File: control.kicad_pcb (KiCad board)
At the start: 2 copper layers, 182 parts, among them J1 Wurth_THR_Terminal_M4, J10 TE_Faston_20-16AWG_Straight_T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, J11 TE_Faston_20-16AWG_Straight_T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, J12 TE_Faston_20-16AWG_Straight_T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, J13 TE_Faston_20-16AWG_Straight_T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, J14 TE_Faston_20-16AWG_Straight_T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, J15 TE_Faston_20-16AWG_Straight_T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, J16 TE_Faston_20-16AWG_Straight_T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, J17 TE_Faston_20-16AWG_Straight_T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, J18 TE_Faston_20-16AWG_Straight_T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, J19 TE_Faston_20-16AWG_Straight_T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, J2 Wurth_THR_Terminal_M4, J20 TE_Faston_20-16AWG_Straight_T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, J21 TE_Faston_20-16AWG_Straight_T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, J22 TE_Faston_20-16AWG_Straight_T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, J23 TE_Faston_20-16AWG_Straight_T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, J24 TE_Faston_20-16AWG_Straight_T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, J25 TE_Faston_20-16AWG_Straight_T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, J26 TE_Faston_20-16AWG_Straight_T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, J27 TE_Faston_20-16AWG_Straight_T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, J28 TE_Faston_20-16AWG_Straight_T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, J29 TE_Faston_20-16AWG_Straight_T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, J3 Wurth_THR_Terminal_M4, J30 TE_Faston_20-16AWG_Straight_T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, J31 TE_Faston_20-16AWG_Straight_T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, J32 TE_Faston_20-16AWG_Straight_T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, J33 Conn_ARM_JTAG_SWD_10, J34 TE_Faston_20-16AWG_Straight_T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, J35 TE_Faston_20-16AWG_Straight_T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, J36 TE_Faston_20-16AWG_Straight_T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, J37 TE_Faston_20-16AWG_Straight_T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, J38 TE_Faston_20-16AWG_Straight_T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, J39 TE_Faston_20-16AWG_Straight_T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, J4 Conn_01x03, J40 TE_Faston_20-16AWG_Straight_T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, J41 TE_Faston_20-16AWG_Straight_T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, J42 TE_Faston_20-16AWG_Straight_T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, J43 TE_Faston_20-16AWG_Straight_T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, J5 Conn_02x20_Odd_Even, J6 TE_Faston_20-16AWG_Straight_T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, J7 TE_Faston_20-16AWG_Straight_T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, J8 TE_Faston_20-16AWG_Straight_T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, J9 TE_Faston_20-16AWG_Straight_T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, Q1 ZXTN08400BFFCT, SW1 SW_Push, U1 TPS7B8733, U10 VND5160J, U11 VND5160J, U12 TCMT4600, U13 TCMT4600, U14 ATSAMD21J18A-A, U15 TCMT4600, U16 VND5160J, U17 VND5160J, U18 VND5160J, U2 MAX33071, U3 TCMT4600, U4 VND5160J, U5 VND5160J, U6 VND5160J, U7 VND5160J, U8 VND5160J, U9 VND5160J, Y1 Crystal

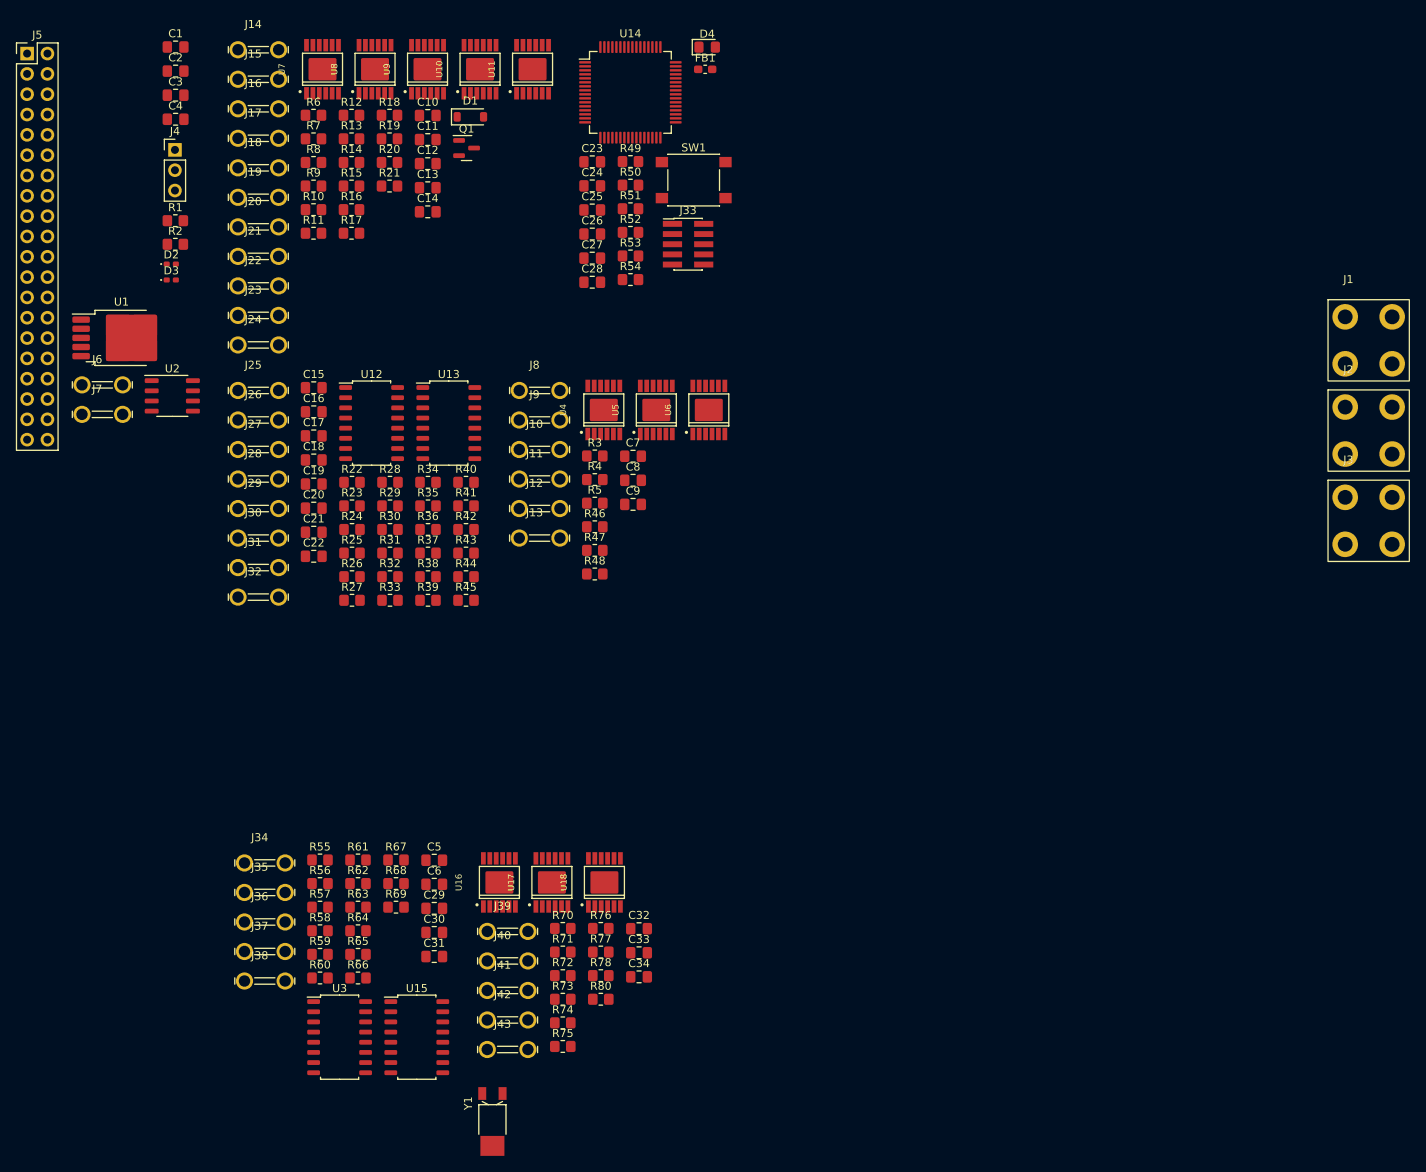
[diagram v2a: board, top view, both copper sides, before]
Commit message: connect signals to connectors, start layout
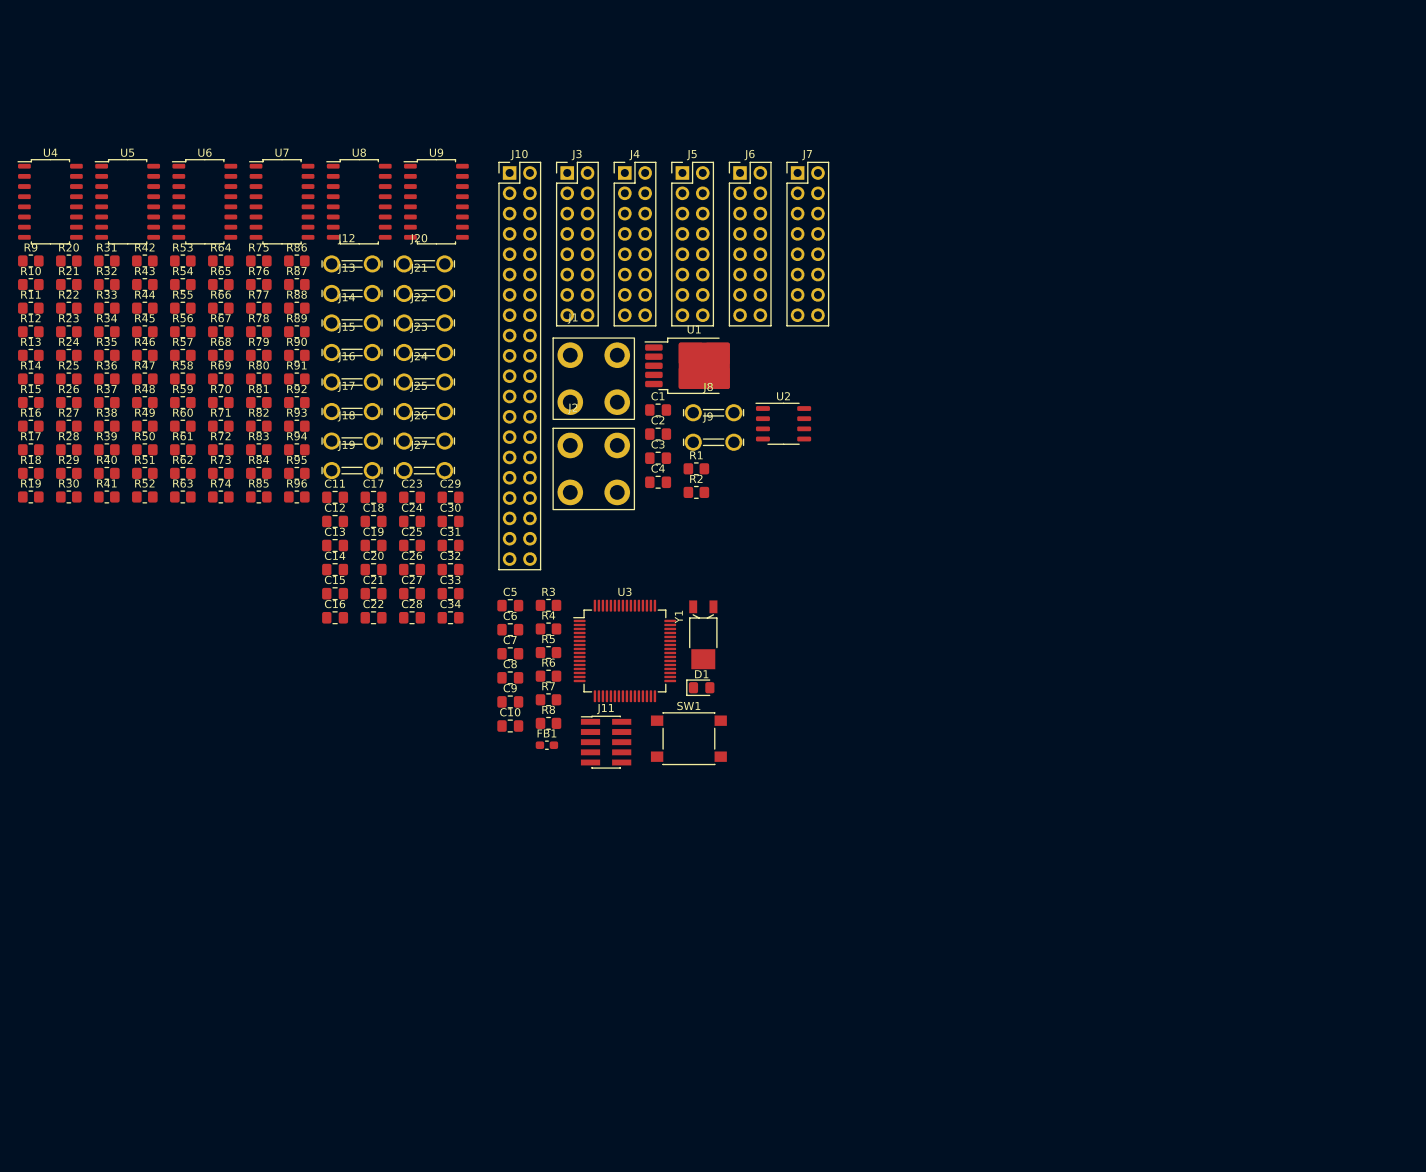
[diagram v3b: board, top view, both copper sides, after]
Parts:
- removed D2, D3: D15V0HA1U2LP-7B, Diode_SMD:D_0402_1005Metric_Pad0.77x0.64mm_HandSolder
- removed D4: LED, LED_SMD:LED_0805_2012Metric_Pad1.15x1.40mm_HandSolder
- removed J28, J29, J30, J31, J32, J34, J35, J36, J37, J38, J39, J40, J41, J42, J43: TE_Faston_20-16AWG_Straight_Tab, Toadly:TE_Faston_20-16AWG_Straight_Tab
- removed J33: Conn_ARM_JTAG_SWD_10, Connector_PinHeader_1.27mm:PinHeader_2x05_P1.27mm_Vertical_SMD
- removed Q1: ZXTN08400BFFCT, Package_TO_SOT_SMD:SOT-23
- removed U10, U11, U16, U17, U18: VND5160J, Toadly:POWERSSO-12
- removed U12, U13, U15: TCMT4600, Package_SO:SOP-16_4.55x10.3mm_P1.27mm
- removed U14: ATSAMD21J18A-A, Package_QFP:TQFP-64_10x10mm_P0.5mm
- added R79: DNP, Resistor_SMD:R_0805_2012Metric_Pad1.20x1.40mm_HandSolder, F.Cu at (-81.4, 43.0)
- added R81: DNP, Resistor_SMD:R_0805_2012Metric_Pad1.20x1.40mm_HandSolder, F.Cu at (-81.4, 48.9)
- added R82: 3.3k, Resistor_SMD:R_0805_2012Metric_Pad1.20x1.40mm_HandSolder, F.Cu at (-81.4, 51.8)
- added R83: 3.3k, Resistor_SMD:R_0805_2012Metric_Pad1.20x1.40mm_HandSolder, F.Cu at (-81.4, 54.8)
- added R84: 3.3k, Resistor_SMD:R_0805_2012Metric_Pad1.20x1.40mm_HandSolder, F.Cu at (-81.4, 57.7)
- added R85: DNP, Resistor_SMD:R_0805_2012Metric_Pad1.20x1.40mm_HandSolder, F.Cu at (-81.4, 60.7)
- added R86: 1.1k, Resistor_SMD:R_0805_2012Metric_Pad1.20x1.40mm_HandSolder, F.Cu at (-76.6, 31.2)
- added R87: DNP, Resistor_SMD:R_0805_2012Metric_Pad1.20x1.40mm_HandSolder, F.Cu at (-76.6, 34.1)
- added R88: 1.1k, Resistor_SMD:R_0805_2012Metric_Pad1.20x1.40mm_HandSolder, F.Cu at (-76.6, 37.1)
- added R89: DNP, Resistor_SMD:R_0805_2012Metric_Pad1.20x1.40mm_HandSolder, F.Cu at (-76.6, 40.0)
- added R90: 1.1k, Resistor_SMD:R_0805_2012Metric_Pad1.20x1.40mm_HandSolder, F.Cu at (-76.6, 43.0)
- added R91: DNP, Resistor_SMD:R_0805_2012Metric_Pad1.20x1.40mm_HandSolder, F.Cu at (-76.6, 45.9)
- added R92: 1.1k, Resistor_SMD:R_0805_2012Metric_Pad1.20x1.40mm_HandSolder, F.Cu at (-76.6, 48.9)
- added R93: DNP, Resistor_SMD:R_0805_2012Metric_Pad1.20x1.40mm_HandSolder, F.Cu at (-76.6, 51.8)
- added R94: 1.1k, Resistor_SMD:R_0805_2012Metric_Pad1.20x1.40mm_HandSolder, F.Cu at (-76.6, 54.8)
- added R95: DNP, Resistor_SMD:R_0805_2012Metric_Pad1.20x1.40mm_HandSolder, F.Cu at (-76.6, 57.7)
- added R96: 1.1k, Resistor_SMD:R_0805_2012Metric_Pad1.20x1.40mm_HandSolder, F.Cu at (-76.6, 60.7)
- C10: value DNP -> 10uF/16V
- C11, C12, C13, C14, C32, C33, C34: value DNP -> 1uF
- C23, C24, C28: value 0.1uF -> 1uF
- C25, C26: value 6.8pF -> 1uF
- C27: value 10uF/16V -> 1uF
- C5, C6: value 1uF -> 6.8pF
- C7, C8, C9: value DNP -> 0.1uF
- D1: value 1N4148W -> LED; footprint Diode_SMD:D_SOD-123 -> LED_SMD:LED_0805_2012Metric_Pad1.15x1.40mm_HandSolder
- J10: value TE_Faston_20-16AWG_Straight_Tab -> Conn_02x20_Odd_Even; footprint Toadly:TE_Faston_20-16AWG_Straight_Tab -> Connector_PinHeader_2.54mm:PinHeader_2x20_P2.54mm_Vertical
- J11: value TE_Faston_20-16AWG_Straight_Tab -> Conn_ARM_JTAG_SWD_10; footprint Toadly:TE_Faston_20-16AWG_Straight_Tab -> Connector_PinHeader_1.27mm:PinHeader_2x05_P1.27mm_Vertical_SMD
- J3: value Wurth_THR_Terminal_M4 -> Conn_02x08_Odd_Even; footprint Toadly:Wurth_THR_Terminal_M4 -> Connector_PinHeader_2.54mm:PinHeader_2x08_P2.54mm_Vertical
- J4: value Conn_01x03 -> Conn_02x08_Odd_Even; footprint Connector_PinHeader_2.54mm:PinHeader_1x03_P2.54mm_Vertical -> Connector_PinHeader_2.54mm:PinHeader_2x08_P2.54mm_Vertical
- J5: value Conn_02x20_Odd_Even -> Conn_02x08_Odd_Even; footprint Connector_PinHeader_2.54mm:PinHeader_2x20_P2.54mm_Vertical -> Connector_PinHeader_2.54mm:PinHeader_2x08_P2.54mm_Vertical
- J6, J7: value TE_Faston_20-16AWG_Straight_Tab -> Conn_02x08_Odd_Even; footprint Toadly:TE_Faston_20-16AWG_Straight_Tab -> Connector_PinHeader_2.54mm:PinHeader_2x08_P2.54mm_Vertical
- R1: value 120 -> 10K
- R10, R11, R12, R15, R16, R75, R77, R78, R9: value 10k -> 3.3k
- R13, R14, R17, R19, R21, R47, R5, R71, R73, R74, R76, R80: value 10k -> DNP
- R18, R20, R46, R48, R70, R72: value 10k -> 1.1k
- R2: value 10K -> 120
- R22, R24: value 3.3k -> 1.1k
- R23, R25, R34, R37, R67: value 3.3k -> DNP
- R26, R28, R38, R40, R42, R44, R68: value DNP -> 1.1k
- R27, R33, R39, R41, R43, R45, R69: value 1.1k -> DNP
- R29, R31, R60: value 1.1k -> 3.3k
- R3: value 10k -> 100K
- R30, R32, R59: value DNP -> 3.3k
- R4, R7: value 10k -> 39
- R49, R54: value 39 -> DNP
- R50: value 0 -> DNP
- R52: value 91 -> DNP
- R53: value 100K -> DNP
- R6: value 10k -> 0
- R8: value 10k -> 91
- U3: value TCMT4600 -> ATSAMD21J18A-A; footprint Package_SO:SOP-16_4.55x10.3mm_P1.27mm -> Package_QFP:TQFP-64_10x10mm_P0.5mm
- U4, U5, U6, U7, U8, U9: value VND5160J -> TCMT4600; footprint Toadly:POWERSSO-12 -> Package_SO:SOP-16_4.55x10.3mm_P1.27mm
- moved J3 109.2 mm to (-42.8, 20.2)
- moved R75 105.3 mm to (-81.4, 31.2)
- moved J1 97.0 mm to (-39.5, 45.9)
- moved J2 97.0 mm to (-39.5, 57.2)
- moved J7 92.0 mm to (-14.0, 20.2)
- moved R76 91.1 mm to (-81.4, 34.1)
- moved R77 91.1 mm to (-81.4, 37.1)
- moved R78 91.1 mm to (-81.4, 40.0)
- moved R80 88.5 mm to (-81.4, 45.9)
- moved FB1 86.8 mm to (-45.4, 91.7)
- moved R64 85.5 mm to (-86.1, 31.2)
- moved R65 85.5 mm to (-86.1, 34.1)
- moved R66 85.5 mm to (-86.1, 37.1)
- moved J6 84.0 mm to (-21.2, 20.2)
- moved J5 83.3 mm to (-28.4, 20.2)
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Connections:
- C10 pad 1: +12C -> GNDREF
- C10 pad 2: GNDREF -> Net-(U3-VDDANA)
- C11 pad 1: +12C -> STOP_LIGHT_SENSE
- C12 pad 1: +12C -> PARK_BRAKE_SENSE
- C13 pad 1: +12C -> MARKER_LIGHT_SENSE
- C14 pad 1: +12C -> REVERSE_LIGHT_SENSE
- C15 pad 1: /Signals/STOP_LIGHT_SENSE -> CAB_2_SENSE
- C16 pad 1: /Signals/PARK_BRAKE_SENSE -> CAB_1_SENSE
- C17 pad 1: /Signals/MARKER_LIGHT_SENSE -> HORN_SENSE
- C18 pad 1: /Signals/REVERSE_LIGHT_SENSE -> AUX_1_SENSE
- C19 pad 1: /Signals/REAR_DOOR_SENSE -> AUX_2_SENSE
- C20 pad 1: /Signals/SIDE_DOOR_SENSE -> BATT_SW_SENSE
- C21 pad 1: /Signals/HORN_SENSE -> CAB_4_SENSE
- C22 pad 1: /Signals/BATT_SW_SENSE -> CAB_3_SENSE
- C23 pad 1: +3.3V -> CAB_6_SENSE
- C24 pad 1: Net-(U14-VDDCORE) -> CAB_5_SENSE
- C25 pad 1: GNDREF -> REAR_DOOR_SENSE
- C25 pad 2: Net-(U14-PA00) -> GNDREF
- C26 pad 1: GNDREF -> COMP_5_SENSE
- C26 pad 2: Net-(U14-PA01) -> GNDREF
- C27 pad 1: GNDREF -> COMP_1_SENSE
- C27 pad 2: Net-(U14-VDDANA) -> GNDREF
- C28 pad 1: GNDREF -> COMP_2_SENSE
- C28 pad 2: Net-(U14-VDDANA) -> GNDREF
- C29 pad 1: /Signals/COMP_2_SENSE -> CAB_8_SENSE
- C30 pad 1: /Signals/COMP_3_SENSE -> CAB_7_SENSE
- C31 pad 1: /Signals/COMP_5_SENSE -> AUX_3_SENSE
- C32 pad 1: +12V -> SIDE_DOOR_SENSE
- C33 pad 1: +12V -> COMP_4_SENSE
- C34 pad 1: +12V -> COMP_3_SENSE
- C5 pad 1: /Signals/COMP_4_SENSE -> GNDREF
- C5 pad 2: GNDREF -> Net-(U3-PA01)
- C6 pad 1: /Signals/COMP_1_SENSE -> GNDREF
- C6 pad 2: GNDREF -> Net-(U3-PA00)
- C7 pad 1: +12V -> Net-(U3-VDDCORE)
- C8 pad 1: +12V -> +3.3V
- C9 pad 1: +12V -> GNDREF
- C9 pad 2: GNDREF -> Net-(U3-VDDANA)
- D1 pad 1: +12C -> Net-(D1-K)
- FB1 pad 1: Net-(U14-VDDANA) -> Net-(U3-VDDANA)
- J10 pad 1: Net-(J10-P1-Pad1) -> +12V
- J10 pad 2: Net-(J10-P1-Pad1) -> +12V
- J11 pad 1: Net-(J11-P1-Pad1) -> Net-(J11-VTref)
- J11 pad 2: Net-(J11-P1-Pad1) -> /MCU/SWDIO
- J2 pad 1: +12C -> GNDREF
- J20 pad 1: Net-(D1-A) -> Net-(J20-P1-Pad1)
- J20 pad 2: Net-(D1-A) -> Net-(J20-P1-Pad1)
- J3 pad 1: GNDREF -> unconnected-(J3-Pin_1-Pad1)
- J4 pad 1: /HORN_SENSE -> unconnected-(J4-Pin_1-Pad1)
- J4 pad 2: /Truck Drivers/HORN_EN -> unconnected-(J4-Pin_2-Pad2)
- J4 pad 3: /HORN_CTL -> unconnected-(J4-Pin_3-Pad3)
- J5 pad 1: +12V -> unconnected-(J5-Pin_1-Pad1)
- J5 pad 10: /RS485_B -> COMP_3_LGT_EN
- J5 pad 12: unconnected-(J5-Pin_12-Pad12) -> COMP_4_LGT_EN
- J5 pad 14: unconnected-(J5-Pin_14-Pad14) -> COMP_5_LGT_EN
- J5 pad 2: +12V -> unconnected-(J5-Pin_2-Pad2)
- J5 pad 3: +12V -> unconnected-(J5-Pin_3-Pad3)
- J5 pad 4: +12V -> unconnected-(J5-Pin_4-Pad4)
- J5 pad 5: GNDREF -> unconnected-(J5-Pin_5-Pad5)
- J5 pad 6: GNDREF -> COMP_1_LGT_EN
- J5 pad 7: GNDREF -> unconnected-(J5-Pin_7-Pad7)
- J5 pad 8: GNDREF -> COMP_2_LGT_EN
- J5 pad 9: /RS485_A -> unconnected-(J5-Pin_9-Pad9)
- J6 pad 1: /RS485_A -> unconnected-(J6-Pin_1-Pad1)
- J6 pad 2: /RS485_A -> unconnected-(J6-Pin_2-Pad2)
- J7 pad 1: /RS485_B -> unconnected-(J7-Pin_1-Pad1)
- J7 pad 2: /RS485_B -> unconnected-(J7-Pin_2-Pad2)
- J8 pad 1: Net-(J8-P1-Pad1) -> /RS485_A
- J8 pad 2: Net-(J8-P1-Pad1) -> /RS485_A
- J9 pad 1: Net-(J9-P1-Pad1) -> /RS485_B
- J9 pad 2: Net-(J9-P1-Pad1) -> /RS485_B
- R1 pad 1: /RS485_A -> RS485_DATA_ENABLE
- R1 pad 2: /RS485_B -> GNDREF
- R10 pad 1: GNDREF -> Net-(J13-P1-Pad1)
- R10 pad 2: /Truck Drivers/INTERSECT_P_EN -> Net-(R10-Pad2)
- R11 pad 1: /Truck Drivers/FOG_EN -> Net-(J14-P1-Pad1)
- R11 pad 2: Net-(U8B-EN) -> Net-(R11-Pad2)
- R12 pad 1: /Truck Drivers/CHIME_EN -> Net-(J15-P1-Pad1)
- R12 pad 2: Net-(U7B-EN) -> Net-(R12-Pad2)
- R13 pad 1: /Truck Drivers/BACKUP_EN -> Net-(R13-Pad1)
- R13 pad 2: Net-(U7C-EN) -> CAB_SIGNAL_2
- R14 pad 1: /Truck Drivers/INTERSECT_D_EN -> Net-(R14-Pad1)
- R14 pad 2: Net-(U9B-EN) -> CAB_SIGNAL_1
- R15 pad 1: /Truck Drivers/INTERSECT_P_EN -> Net-(R13-Pad1)
- R15 pad 2: Net-(U9C-EN) -> +12V
- R16 pad 1: /Truck Drivers/HORN_EN -> Net-(R14-Pad1)
- R16 pad 2: Net-(Q1-B) -> +12V
- R17 pad 1: GNDREF -> STOP_LIGHT_SENSE
- R17 pad 2: /Truck Drivers/MARKER_EN -> +3.3V
- R18 pad 2: /Truck Drivers/HEADLIGHT_EN -> STOP_LIGHT_SENSE
- R19 pad 1: Net-(Q1-B) -> PARK_BRAKE_SENSE
- R19 pad 2: GNDREF -> +3.3V
- R2 pad 1: /MCU/RS485_DATA_ENABLE -> /RS485_A
- R2 pad 2: GNDREF -> /RS485_B
- R20 pad 1: /Truck Drivers/MARKER_EN -> GNDREF
- R20 pad 2: Net-(U10B-EN) -> PARK_BRAKE_SENSE
- R21 pad 1: /Truck Drivers/HEADLIGHT_EN -> MARKER_LIGHT_SENSE
- R21 pad 2: Net-(U11B-EN) -> +3.3V
- R22 pad 1: Net-(J25-P1-Pad1) -> GNDREF
- R22 pad 2: Net-(R22-Pad2) -> MARKER_LIGHT_SENSE
- R23 pad 1: Net-(J26-P1-Pad1) -> REVERSE_LIGHT_SENSE
- R23 pad 2: Net-(R23-Pad2) -> +3.3V
- R24 pad 1: Net-(J27-P1-Pad1) -> GNDREF
- R24 pad 2: Net-(R24-Pad2) -> REVERSE_LIGHT_SENSE
- R25 pad 1: Net-(J28-P1-Pad1) -> CAB_2_SENSE
- R25 pad 2: Net-(R25-Pad2) -> +3.3V
- R26 pad 1: /Signals/STOP_LIGHT_SENSE -> GNDREF
- R26 pad 2: +3.3V -> CAB_2_SENSE
- R27 pad 1: GNDREF -> CAB_1_SENSE
- R27 pad 2: /Signals/STOP_LIGHT_SENSE -> +3.3V
- R28 pad 1: /Signals/PARK_BRAKE_SENSE -> GNDREF
- R28 pad 2: +3.3V -> CAB_1_SENSE
- R29 pad 1: GNDREF -> Net-(J16-P1-Pad1)
- R29 pad 2: /Signals/PARK_BRAKE_SENSE -> Net-(R29-Pad2)
- R3 pad 1: /Drivers/FLOOD_D_EN -> /MCU/#RESET
- R3 pad 2: Net-(U4B-EN) -> +3.3V
- R30 pad 1: /Signals/MARKER_LIGHT_SENSE -> Net-(J17-P1-Pad1)
- R30 pad 2: +3.3V -> Net-(R30-Pad2)
- R31 pad 1: GNDREF -> Net-(J18-P1-Pad1)
- R31 pad 2: /Signals/MARKER_LIGHT_SENSE -> Net-(R31-Pad2)
- R32 pad 1: /Signals/REVERSE_LIGHT_SENSE -> Net-(J19-P1-Pad1)
- R32 pad 2: +3.3V -> Net-(R32-Pad2)
- R33 pad 1: GNDREF -> Net-(R33-Pad1)
- R33 pad 2: /Signals/REVERSE_LIGHT_SENSE -> CAB_SIGNAL_4
- R34 pad 1: Net-(J29-P1-Pad1) -> Net-(R34-Pad1)
- R34 pad 2: Net-(R34-Pad2) -> CAB_SIGNAL_3
- R35 pad 1: Net-(J30-P1-Pad1) -> Net-(R33-Pad1)
- R35 pad 2: Net-(R35-Pad2) -> +12V
- R36 pad 1: /Signals/HORN_SIGNAL -> Net-(R34-Pad1)
- R36 pad 2: Net-(R36-Pad2) -> +12V
- R37 pad 1: Net-(J32-P1-Pad1) -> HORN_SENSE
- R37 pad 2: Net-(R37-Pad2) -> +3.3V
- R38 pad 1: /Signals/REAR_DOOR_SENSE -> GNDREF
- R38 pad 2: +3.3V -> HORN_SENSE
- R39 pad 1: GNDREF -> AUX_1_SENSE
- R39 pad 2: /Signals/REAR_DOOR_SENSE -> +3.3V
- R4 pad 1: /Drivers/FLOOD_R_EN -> Net-(R4-Pad1)
- R4 pad 2: Net-(U5B-EN) -> /MCU/#RESET
- R40 pad 1: /Signals/SIDE_DOOR_SENSE -> GNDREF
- R40 pad 2: +3.3V -> AUX_1_SENSE
- R41 pad 1: GNDREF -> AUX_2_SENSE
- R41 pad 2: /Signals/SIDE_DOOR_SENSE -> +3.3V
- R42 pad 1: /Signals/HORN_SENSE -> GNDREF
- R42 pad 2: +3.3V -> AUX_2_SENSE
- R43 pad 1: GNDREF -> BATT_SW_SENSE
- R43 pad 2: /Signals/HORN_SENSE -> +3.3V
- R44 pad 1: /Signals/BATT_SW_SENSE -> GNDREF
- R44 pad 2: +3.3V -> BATT_SW_SENSE
- R45 pad 1: GNDREF -> CAB_4_SENSE
- R45 pad 2: /Signals/BATT_SW_SENSE -> +3.3V
- R46 pad 2: /Drivers/FLOOD_D_EN -> CAB_4_SENSE
- R47 pad 1: GNDREF -> CAB_3_SENSE
- R47 pad 2: /Drivers/FLOOD_R_EN -> +3.3V
- R48 pad 2: /Drivers/FLOOD_P_EN -> CAB_3_SENSE
- R49 pad 1: Net-(J33-~{RESET}) -> Net-(R49-Pad1)
- R49 pad 2: /MCU/#RESET -> CAB_SIGNAL_6
- R5 pad 1: /Drivers/FLOOD_P_EN -> Net-(J11-VTref)
- R5 pad 2: Net-(U6B-EN) -> GNDREF
- R50 pad 1: Net-(J33-VTref) -> Net-(R50-Pad1)
- R50 pad 2: +3.3V -> CAB_SIGNAL_5
- R51 pad 1: Net-(J33-VTref) -> Net-(R51-Pad1)
- R51 pad 2: GNDREF -> Net-(J22-P1-Pad1)
- R52 pad 1: Net-(D4-A) -> Net-(R52-Pad1)
- R52 pad 2: +3.3V -> Net-(J20-P1-Pad1)
- R53 pad 1: /MCU/#RESET -> Net-(R53-Pad1)
- R53 pad 2: +3.3V -> Net-(J21-P1-Pad1)
- R54 pad 2: /MCU/#RESET -> Net-(J23-P1-Pad1)
- R55 pad 1: Net-(J34-P1-Pad1) -> Net-(R49-Pad1)
- R56 pad 1: Net-(J35-P1-Pad1) -> Net-(R50-Pad1)
- R57 pad 1: Net-(J36-P1-Pad1) -> Net-(R51-Pad1)
- R58 pad 1: Net-(J37-P1-Pad1) -> Net-(R54-Pad1)
- R59 pad 1: /Signals/COMP_4_SENSE -> Net-(R52-Pad1)
- R59 pad 2: +3.3V -> +12V
- R6 pad 1: GNDREF -> Net-(J11-VTref)
- R6 pad 2: /Truck Drivers/FOG_EN -> +3.3V
- R60 pad 1: GNDREF -> Net-(R53-Pad1)
- R60 pad 2: /Signals/COMP_4_SENSE -> +12V
- R61 pad 1: /Signals/COMP_1_SENSE -> CAB_6_SENSE
- R62 pad 2: /Signals/COMP_1_SENSE -> CAB_6_SENSE
- R63 pad 1: /Signals/COMP_2_SENSE -> CAB_5_SENSE
- R64 pad 2: /Signals/COMP_2_SENSE -> CAB_5_SENSE
- R65 pad 1: /Signals/COMP_3_SENSE -> REAR_DOOR_SENSE
- R66 pad 2: /Signals/COMP_3_SENSE -> REAR_DOOR_SENSE
- R67 pad 1: Net-(J38-P1-Pad1) -> COMP_5_SENSE
- R67 pad 2: +12V -> +3.3V
- R68 pad 1: /Signals/COMP_5_SENSE -> GNDREF
- R68 pad 2: +3.3V -> COMP_5_SENSE
- R69 pad 1: GNDREF -> COMP_1_SENSE
- R69 pad 2: /Signals/COMP_5_SENSE -> +3.3V
- R7 pad 1: GNDREF -> Net-(J11-~{RESET})
- R7 pad 2: /Truck Drivers/CHIME_EN -> /MCU/#RESET
- R70 pad 2: /Drivers/COMP_1_LGT_EN -> COMP_1_SENSE
- R71 pad 1: /Drivers/COMP_1_LGT_EN -> COMP_2_SENSE
- R71 pad 2: Net-(U16B-EN) -> +3.3V
- R72 pad 2: /Drivers/COMP_2_LGT_EN -> COMP_2_SENSE
- R73 pad 1: /Drivers/COMP_2_LGT_EN -> Net-(R73-Pad1)
- R73 pad 2: Net-(U16C-EN) -> CAB_SIGNAL_8
- R74 pad 1: GNDREF -> Net-(R74-Pad1)
- R74 pad 2: /Drivers/COMP_3_LGT_EN -> CAB_SIGNAL_7
- R75 pad 1: GNDREF -> Net-(R75-Pad1)
- R75 pad 2: /Drivers/COMP_4_LGT_EN -> Net-(J24-P1-Pad1)
- R76 pad 1: /Drivers/COMP_3_LGT_EN -> Net-(R76-Pad1)
- R76 pad 2: Net-(U17B-EN) -> Net-(J25-P1-Pad1)
- R77 pad 1: /Drivers/COMP_4_LGT_EN -> Net-(R73-Pad1)
- R77 pad 2: Net-(U17C-EN) -> +12V
- R78 pad 1: GNDREF -> Net-(R74-Pad1)
- R78 pad 2: /Drivers/COMP_5_LGT_EN -> +12V
- R8 pad 1: GNDREF -> Net-(D1-A)
- R8 pad 2: /Truck Drivers/BACKUP_EN -> +3.3V
- R80 pad 1: /Drivers/COMP_5_LGT_EN -> Net-(R80-Pad1)
- R80 pad 2: Net-(U18B-EN) -> Net-(J27-P1-Pad1)
- R9 pad 1: GNDREF -> Net-(J12-P1-Pad1)
- R9 pad 2: /Truck Drivers/INTERSECT_D_EN -> Net-(R9-Pad2)
- SW1 pad 2: Net-(R54-Pad1) -> Net-(R4-Pad1)
- U2 pad 1: /RX -> UART3_RX
- U2 pad 2: /MCU/RS485_DATA_ENABLE -> RS485_DATA_ENABLE
- U2 pad 3: /MCU/RS485_DATA_ENABLE -> RS485_DATA_ENABLE
- U2 pad 4: /TX -> UART3_TX
- U3 pad 1: Net-(J35-P1-Pad1) -> Net-(U3-PA00)
- U3 pad 10: +3.3V -> COMP_5_LGT_EN
- U3 pad 11: /Signals/COMP_3_SENSE -> COMP_1_SENSE
- U3 pad 12: +3.3V -> COMP_2_SENSE
- U3 pad 13: /Signals/COMP_2_SENSE -> FOG_LGT_EN
- U3 pad 14: +3.3V -> ISECT_D_EN
- U3 pad 15: /Signals/COMP_1_SENSE -> ISECT_P_EN
- U3 pad 16: +3.3V -> AUX_1_EN
- U3 pad 2: GNDREF -> Net-(U3-PA01)
- U3 pad 3: Net-(J36-P1-Pad1) -> CAB_CHIME_EN
- U3 pad 4: GNDREF -> BACKUP_CHIME_EN
- U3 pad 5: Net-(J37-P1-Pad1) -> COMP_2_LGT_EN
- U3 pad 6: GNDREF -> COMP_3_LGT_EN
- U3 pad 7: Net-(J34-P1-Pad1) -> GNDREF
- U3 pad 8: GNDREF -> Net-(U3-VDDANA)
- U3 pad 9: /Signals/COMP_4_SENSE -> COMP_4_LGT_EN
- U4 pad 1: GNDREF -> Net-(R10-Pad2)
- U4 pad 10: Net-(J8-P1-Pad1) -> +3.3V
- U4 pad 11: Net-(J8-P1-Pad1) -> REVERSE_LIGHT_SENSE
- U4 pad 12: +12V -> +3.3V
- U4 pad 2: unconnected-(U4A-STAT_DIS-Pad2) -> GNDREF
- U4 pad 3: Net-(U4B-EN) -> Net-(R11-Pad2)
- U4 pad 4: unconnected-(U4B-STATUS-Pad4) -> GNDREF
- U4 pad 5: unconnected-(U4C-STATUS-Pad5) -> Net-(R12-Pad2)
- U4 pad 6: Net-(U4B-EN) -> GNDREF
- U4 pad 7: +12V -> Net-(R9-Pad2)
- U4 pad 8: Net-(J9-P1-Pad1) -> GNDREF
- U4 pad 9: Net-(J9-P1-Pad1) -> STOP_LIGHT_SENSE
- U5 pad 1: GNDREF -> Net-(R14-Pad1)
- U5 pad 10: Net-(J10-P1-Pad1) -> +3.3V
- U5 pad 11: Net-(J10-P1-Pad1) -> CAB_3_SENSE
- U5 pad 12: +12V -> +3.3V
- U5 pad 2: unconnected-(U5A-STAT_DIS-Pad2) -> GNDREF
- U5 pad 3: Net-(U5B-EN) -> Net-(R13-Pad1)
- U5 pad 4: unconnected-(U5B-STATUS-Pad4) -> GNDREF
- U5 pad 5: unconnected-(U5C-STATUS-Pad5) -> Net-(R34-Pad1)
- U5 pad 6: Net-(U5B-EN) -> GNDREF
- U5 pad 7: +12V -> Net-(R33-Pad1)
- U5 pad 8: Net-(J11-P1-Pad1) -> GNDREF
- U5 pad 9: Net-(J11-P1-Pad1) -> CAB_4_SENSE
- U6 pad 1: GNDREF -> Net-(R32-Pad2)
- U6 pad 10: Net-(J12-P1-Pad1) -> +3.3V
- U6 pad 11: Net-(J12-P1-Pad1) -> AUX_1_SENSE
- U6 pad 12: +12V -> +3.3V
- U6 pad 2: unconnected-(U6A-STAT_DIS-Pad2) -> GNDREF
- U6 pad 3: Net-(U6B-EN) -> Net-(R29-Pad2)
- U6 pad 4: unconnected-(U6B-STATUS-Pad4) -> GNDREF
- U6 pad 5: unconnected-(U6C-STATUS-Pad5) -> Net-(R30-Pad2)
- U6 pad 6: Net-(U6B-EN) -> GNDREF
- U6 pad 7: +12V -> Net-(R31-Pad2)
- U6 pad 8: Net-(J13-P1-Pad1) -> GNDREF
- U6 pad 9: Net-(J13-P1-Pad1) -> AUX_2_SENSE
- U7 pad 1: GNDREF -> Net-(R50-Pad1)
- U7 pad 10: Net-(J16-P1-Pad1) -> +3.3V
- U7 pad 11: Net-(J16-P1-Pad1) -> CAB_7_SENSE
- U7 pad 12: +12C -> +3.3V
- U7 pad 2: unconnected-(U7A-STAT_DIS-Pad2) -> GNDREF
- U7 pad 3: Net-(U7B-EN) -> Net-(R49-Pad1)
- U7 pad 4: unconnected-(U7B-STATUS-Pad4) -> GNDREF
- U7 pad 5: unconnected-(U7C-STATUS-Pad5) -> Net-(R74-Pad1)
- U7 pad 6: Net-(U7C-EN) -> GNDREF
- U7 pad 7: +12C -> Net-(R73-Pad1)
- U7 pad 8: Net-(J17-P1-Pad1) -> GNDREF
- U7 pad 9: Net-(J17-P1-Pad1) -> CAB_8_SENSE
- U8 pad 1: GNDREF -> Net-(R54-Pad1)
- U8 pad 10: Net-(J14-P1-Pad1) -> +3.3V
- U8 pad 11: Net-(J14-P1-Pad1) -> SIDE_DOOR_SENSE
- U8 pad 12: +12C -> +3.3V
- U8 pad 2: unconnected-(U8A-STAT_DIS-Pad2) -> GNDREF
- U8 pad 3: Net-(U8B-EN) -> Net-(R51-Pad1)
- U8 pad 4: unconnected-(U8B-STATUS-Pad4) -> GNDREF
- U8 pad 5: unconnected-(U8C-STATUS-Pad5) -> Net-(R76-Pad1)
- U8 pad 6: Net-(U8B-EN) -> GNDREF
- U8 pad 7: +12C -> Net-(R75-Pad1)
- U8 pad 8: Net-(J15-P1-Pad1) -> GNDREF
- U8 pad 9: Net-(J15-P1-Pad1) -> AUX_3_SENSE
- U9 pad 1: GNDREF -> Net-(R52-Pad1)
- U9 pad 10: Net-(J18-P1-Pad1) -> +3.3V
- U9 pad 11: Net-(J18-P1-Pad1) -> COMP_3_SENSE
- U9 pad 12: +12C -> +3.3V
- U9 pad 2: unconnected-(U9A-STAT_DIS-Pad2) -> GNDREF
- U9 pad 3: Net-(U9B-EN) -> Net-(R53-Pad1)
- U9 pad 4: unconnected-(U9B-STATUS-Pad4) -> GNDREF
- U9 pad 5: unconnected-(U9C-STATUS-Pad5) -> Net-(R80-Pad1)
- U9 pad 6: Net-(U9C-EN) -> GNDREF
- U9 pad 7: +12C -> Net-(R79-Pad1)
- U9 pad 8: Net-(J19-P1-Pad1) -> GNDREF
- U9 pad 9: Net-(J19-P1-Pad1) -> COMP_4_SENSE
- Y1 pad 1: Net-(U14-PA01) -> Net-(U3-PA01)
- Y1 pad 2: Net-(U14-PA00) -> Net-(U3-PA00)

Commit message: begin grouping parts
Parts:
- removed R6: 0, Resistor_SMD:R_0805_2012Metric_Pad1.20x1.40mm_HandSolder
- added C35: 22uF, Capacitor_SMD:CP_Elec_6.3x7.7, F.Cu at (188.8, 71.2)
- added D2: D, Diode_SMD:D_SMA_Handsoldering, F.Cu at (177.0, 71.1)
- added JP1: Jumper_2_Open, Connector_PinHeader_2.54mm:PinHeader_1x02_P2.54mm_Vertical, F.Cu at (203.4, 85.6)
- Y1: value Crystal -> 32.768kHz
- moved R69 337.7 mm to (232.3, -66.3)
- moved R70 337.7 mm to (232.3, -63.3)
- moved R71 337.7 mm to (232.3, -60.4)
- moved R72 337.7 mm to (232.3, -57.4)
- moved C33 337.1 mm to (248.4, -69.0)
- moved C34 337.1 mm to (248.4, -66.0)
- moved C27 337.1 mm to (243.6, -69.0)
- moved C28 337.1 mm to (243.6, -66.0)
- moved R93 335.7 mm to (237.7, -66.0)
- moved R94 335.7 mm to (237.7, -63.0)
- moved R95 335.7 mm to (237.7, -60.1)
- moved R96 335.7 mm to (237.7, -57.1)
- moved R52 320.2 mm to (200.9, -60.2)
- moved R59 316.0 mm to (205.2, -61.5)
- moved R60 316.0 mm to (205.2, -58.6)
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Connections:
- J1 pad 1: +12V -> Net-(D2-A)
- J7 pad 12: AUX_4_EN -> unconnected-(J7-Pin_12-Pad12)
- J7 pad 14: AUX_5_EN -> unconnected-(J7-Pin_14-Pad14)
- J7 pad 6: unconnected-(J7-Pin_6-Pad6) -> AUX_4_EN
- J7 pad 8: unconnected-(J7-Pin_8-Pad8) -> AUX_5_EN
- Y1 pad 1: Net-(U3-PA01) -> Net-(U3-PA00)
- Y1 pad 2: Net-(U3-PA00) -> Net-(U3-PA01)
- Y1 pad 3: (no net) -> GNDREF
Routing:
- net /RS485_B: track 0.00 -> 16.0 mm
- net /RS485_A: track 0.00 -> 16.0 mm
- net Net-(U3-PA01): track 0.00 -> 11.8 mm
- net Net-(U3-PA00): track 0.00 -> 8.59 mm
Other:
- board outline added: 151.9 x 109.5 mm
- board text added: "RS485 A"
- board text added: "RS485 B"

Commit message: route sense input tracks
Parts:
- added REF**: MountingHole_4.3mm_M4, MountingHole:MountingHole_4.3mm_M4, F.Cu at (75.7, 47.2)
- added REF**: MountingHole_4.3mm_M4, MountingHole:MountingHole_4.3mm_M4, F.Cu at (75.7, 147.1)
- moved C33 223.6 mm to (126.3, 118.2), turned to -90 degrees
- moved C34 218.5 mm to (131.0, 118.2), turned to -90 degrees
- moved R94 214.0 mm to (124.0, 118.2), turned to 90 degrees
- moved C27 213.9 mm to (140.2, 118.2), turned to -90 degrees
- moved C28 213.6 mm to (135.6, 118.2), turned to -90 degrees
- moved R93 211.3 mm to (127.0, 114.0)
- moved R96 206.5 mm to (128.6, 118.2), turned to 90 degrees
- moved R70 204.6 mm to (137.9, 118.2), turned to 90 degrees
- moved R95 202.7 mm to (129.8, 111.5)
- moved R69 202.6 mm to (135.2, 111.5)
- moved R72 201.7 mm to (133.3, 118.2), turned to 90 degrees
- moved R71 200.6 mm to (132.8, 113.8)
- moved R79 198.5 mm to (97.8, 93.1), turned to 180 degrees
- moved U9 190.9 mm to (131.3, 105.8), turned to -90 degrees
- moved R80 190.6 mm to (97.8, 86.1), turned to 180 degrees
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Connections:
- R10 pad 1: Net-(J13-P1-Pad1) -> Net-(J12-P1-Pad1)
- R11 pad 1: Net-(J14-P1-Pad1) -> Net-(J13-P1-Pad1)
- R12 pad 1: Net-(J15-P1-Pad1) -> Net-(J14-P1-Pad1)
- R29 pad 1: Net-(J16-P1-Pad1) -> Net-(J17-P1-Pad1)
- R30 pad 1: Net-(J17-P1-Pad1) -> Net-(J18-P1-Pad1)
- R31 pad 1: Net-(J18-P1-Pad1) -> Net-(J19-P1-Pad1)
- R32 pad 1: Net-(J19-P1-Pad1) -> Net-(J16-P1-Pad1)
- R51 pad 2: Net-(J22-P1-Pad1) -> Net-(J21-P1-Pad1)
- R52 pad 2: Net-(J20-P1-Pad1) -> Net-(J24-P1-Pad1)
- R53 pad 2: Net-(J21-P1-Pad1) -> Net-(J25-P1-Pad1)
- R54 pad 2: Net-(J23-P1-Pad1) -> Net-(J20-P1-Pad1)
- R75 pad 2: Net-(J24-P1-Pad1) -> Net-(J23-P1-Pad1)
- R76 pad 2: Net-(J25-P1-Pad1) -> Net-(J22-P1-Pad1)
- R79 pad 2: Net-(J26-P1-Pad1) -> Net-(J27-P1-Pad1)
- R80 pad 2: Net-(J27-P1-Pad1) -> Net-(J26-P1-Pad1)
- R9 pad 1: Net-(J12-P1-Pad1) -> Net-(J15-P1-Pad1)
- U5 pad 1: Net-(R14-Pad1) -> Net-(R33-Pad1)
- U5 pad 11: CAB_3_SENSE -> CAB_2_SENSE
- U5 pad 13: CAB_2_SENSE -> CAB_3_SENSE
- U5 pad 15: CAB_1_SENSE -> CAB_4_SENSE
- U5 pad 3: Net-(R13-Pad1) -> Net-(R34-Pad1)
- U5 pad 5: Net-(R34-Pad1) -> Net-(R13-Pad1)
- U5 pad 7: Net-(R33-Pad1) -> Net-(R14-Pad1)
- U5 pad 9: CAB_4_SENSE -> CAB_1_SENSE
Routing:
- net +3.3V: track 0.00 -> 92.2 mm
- net Net-(R52-Pad1): track 0.00 -> 54.7 mm
- net Net-(R53-Pad1): track 0.00 -> 49.1 mm
- net Net-(R80-Pad1): track 0.00 -> 41.6 mm
- net Net-(R79-Pad1): track 0.00 -> 38.6 mm
- net Net-(R54-Pad1): track 0.00 -> 31.5 mm
- net Net-(R51-Pad1): track 0.00 -> 30.1 mm
- net Net-(R76-Pad1): track 0.00 -> 27.6 mm
- net CAB_3_SENSE: track 0.00 -> 27.3 mm
- net CAB_4_SENSE: track 0.00 -> 27.3 mm
- net CAB_1_SENSE: track 0.00 -> 26.0 mm
- net CAB_2_SENSE: track 0.00 -> 25.6 mm
- net Net-(R75-Pad1): track 0.00 -> 25.3 mm
- net Net-(J16-P1-Pad1): track 0.00 -> 19.5 mm
- net Net-(J15-P1-Pad1): track 0.00 -> 18.2 mm
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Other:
- board size 151.9 x 109.5 mm -> 151.6 x 109.5 mm
- copper layers 2 -> 4
- board text added: "AUX 1"
- board text added: "AUX 2"
- board text added: "AUX 3"
- board text added: "BATT SW"
- board text added: "COMP 1"
- board text added: "COMP 2"
- board text added: "COMP 3"
- board text added: "COMP 4"
- board text added: "COMP 5"
- board text added: "HORN"
- board text added: "MARKER"
- board text added: "P BRAKE"
- board text added: "R DOOR"
- board text added: "REVERSE"
- board text added: "S DOOR"
- board text added: "STOP"
